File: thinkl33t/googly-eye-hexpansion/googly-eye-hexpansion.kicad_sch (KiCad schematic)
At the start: 11 parts, among them J1 Hexpansion-Connector, U1 ZD24C64A-XGMT

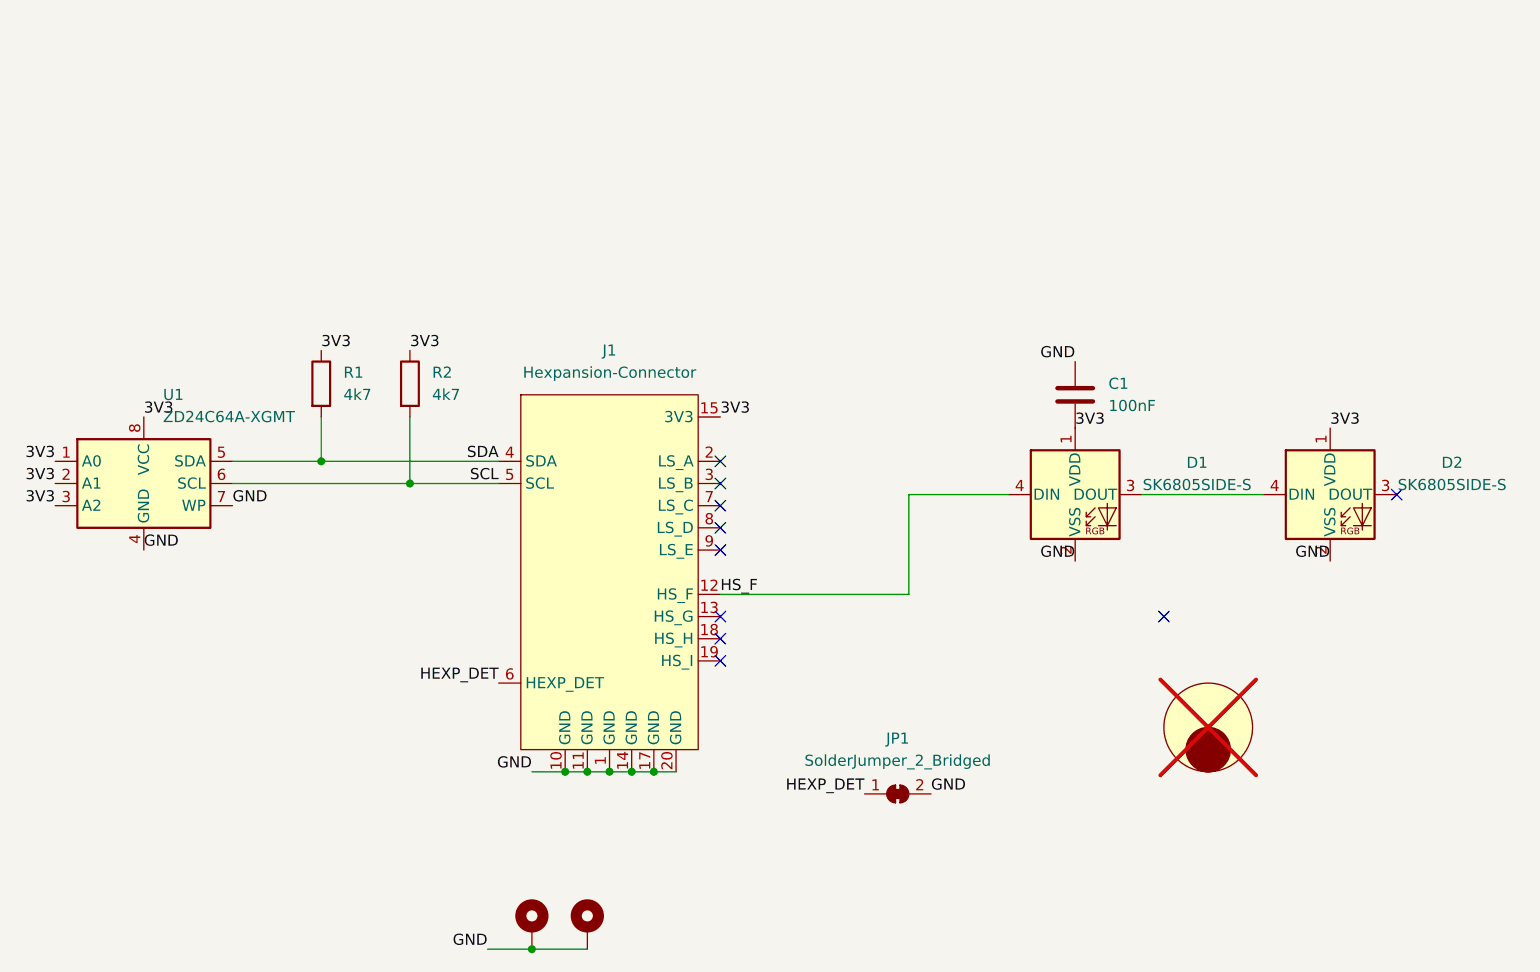
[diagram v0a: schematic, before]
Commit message: Add ap3602 to boost from 3v3 to 5v, as the minimum for the LEDs is 3.5v
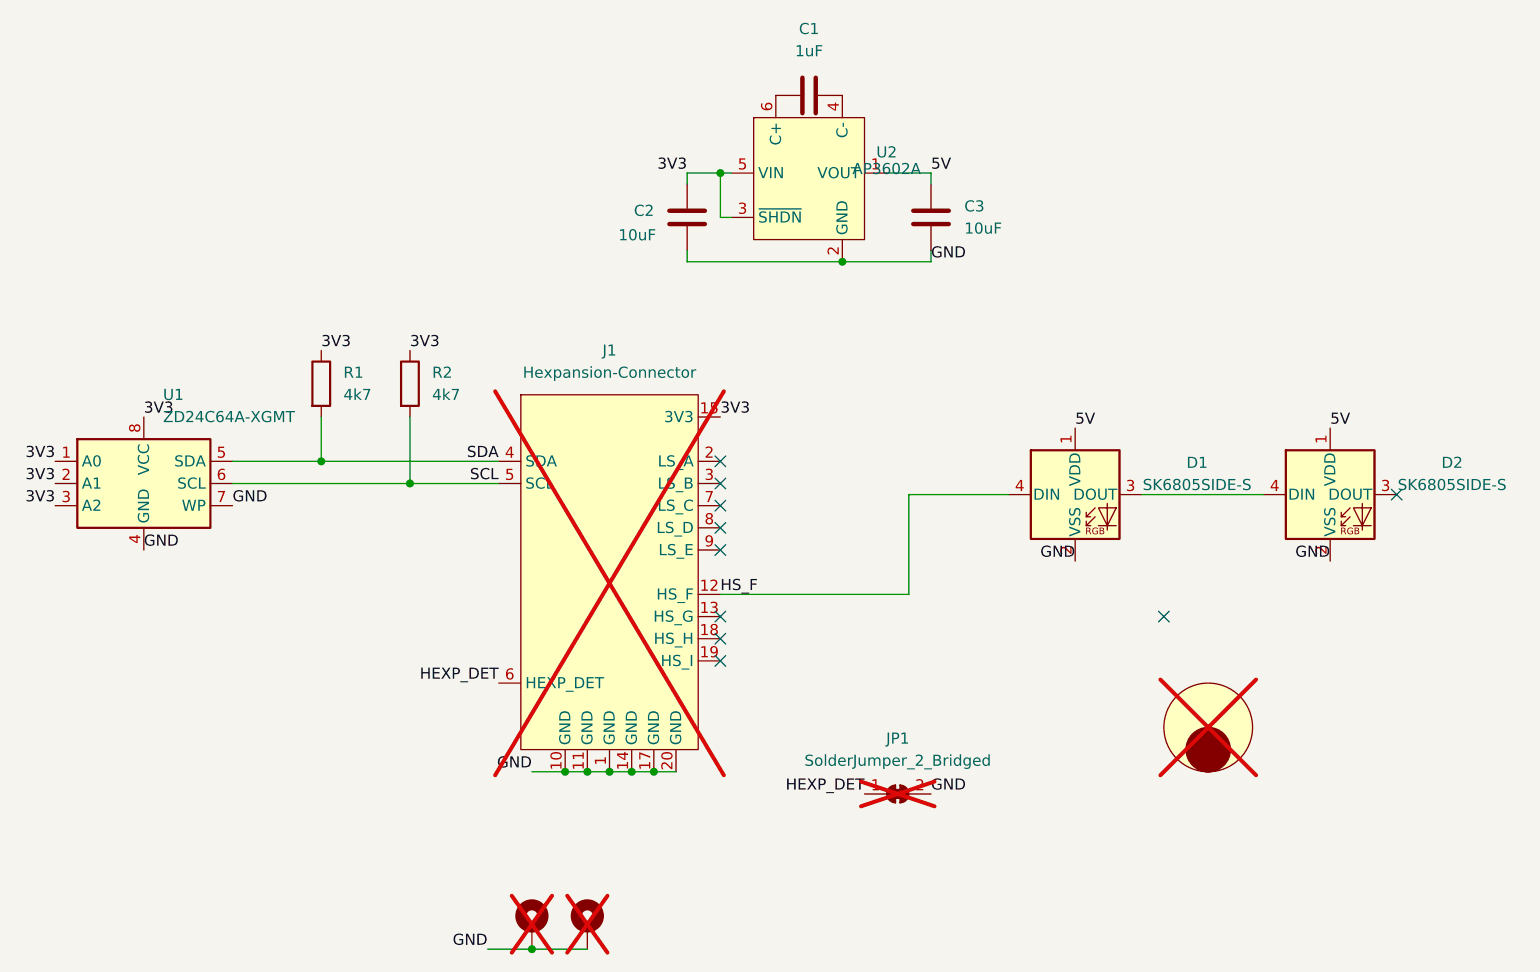
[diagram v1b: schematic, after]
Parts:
- added C2, C3: 10uF, Capacitor_SMD:C_0603_1608Metric, symbol Device:C
- added U2: AP3602A, Package_TO_SOT_SMD:TSOT-23-6_HandSoldering, symbol AP3602:AP3602A
- C1: value 100nF -> 1uF; footprint Capacitor_SMD:C_0805_2012Metric -> Capacitor_SMD:C_0402_1005Metric; MPN C49678 -> C2887021
- H1, H2, J1, JP1: now not fitted
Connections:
- net 3V3: now also C2.2, U2.3 (~{SHDN}), U2.5 (VIN); no longer C1.2, D1.1 (VDD), D2.1 (VDD)
- net GND: now also C2.1, C3.1, U2.2 (GND); no longer C1.1
- new net: C1.1, U2.6 (C+)
- new net: C1.2, U2.4 (C-)
- new net 5V: C3.2, D1.1 (VDD), D2.1 (VDD), U2.1 (VOUT)
